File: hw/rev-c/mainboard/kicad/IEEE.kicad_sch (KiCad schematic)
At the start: 26 parts, among them J10 IEEE_HEADER, J11 IEEE, U14 SN74LS07, U15 SN74LS07, U16 SN74LS07, U17 74LS245, U18 74LS245

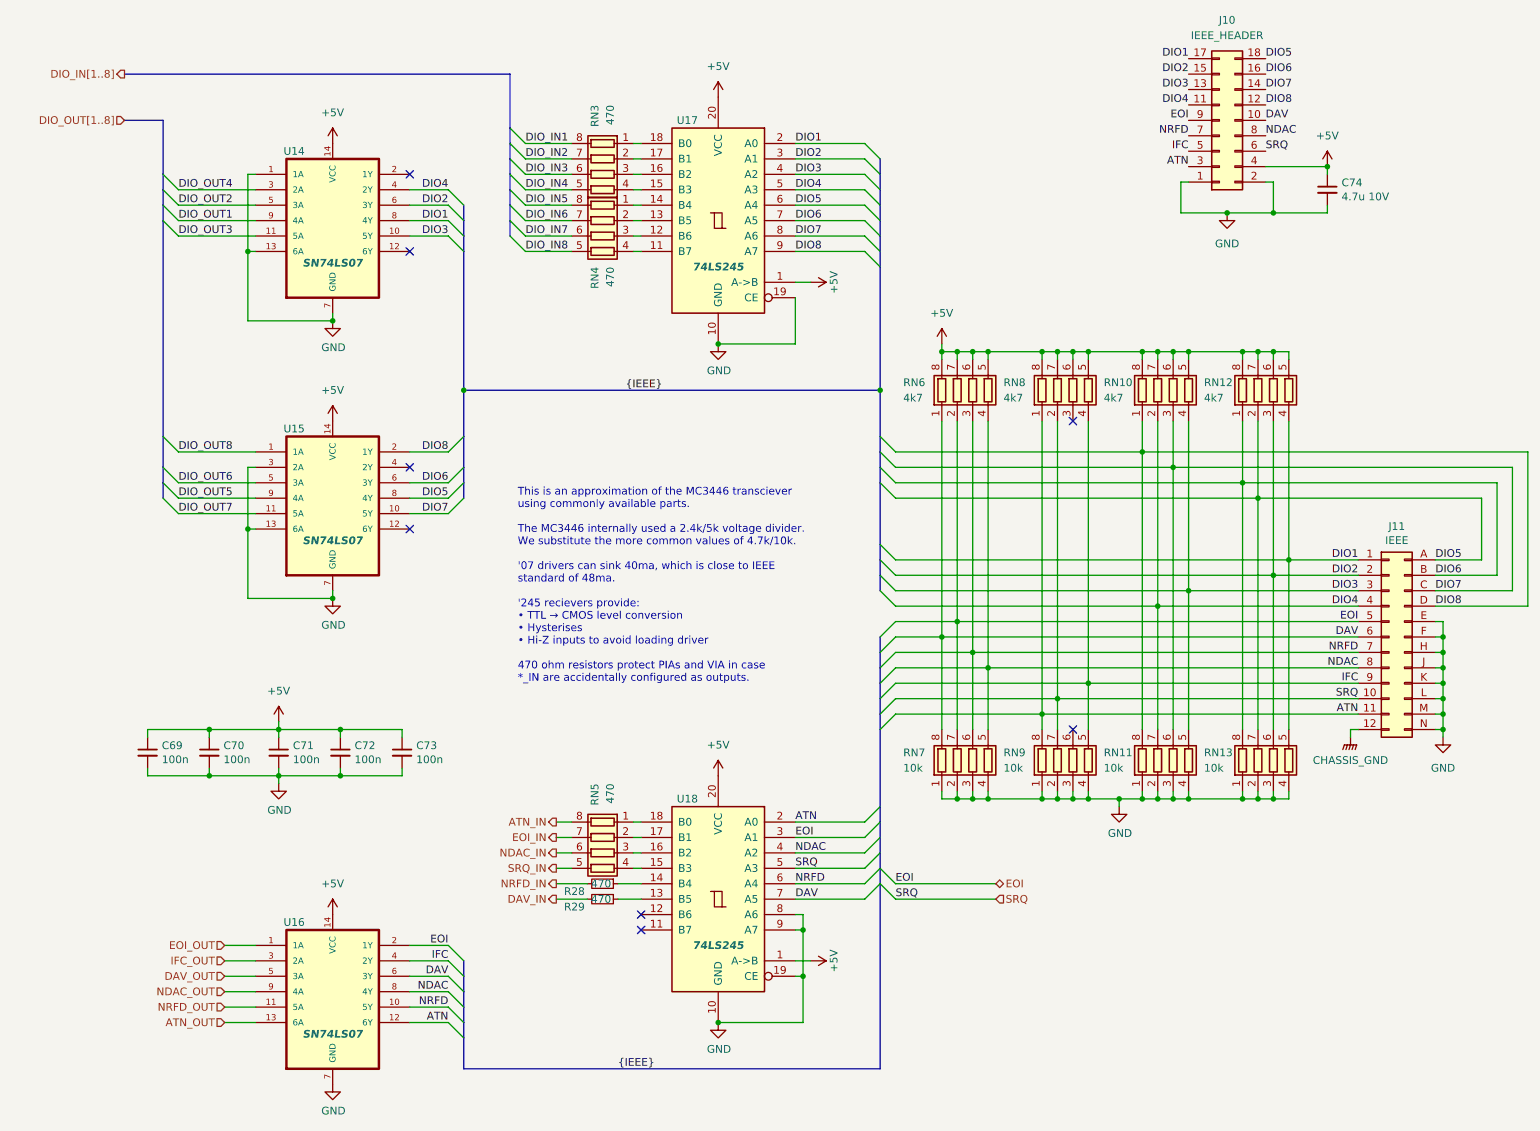
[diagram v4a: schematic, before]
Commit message: hw: match original PET designators for connectors
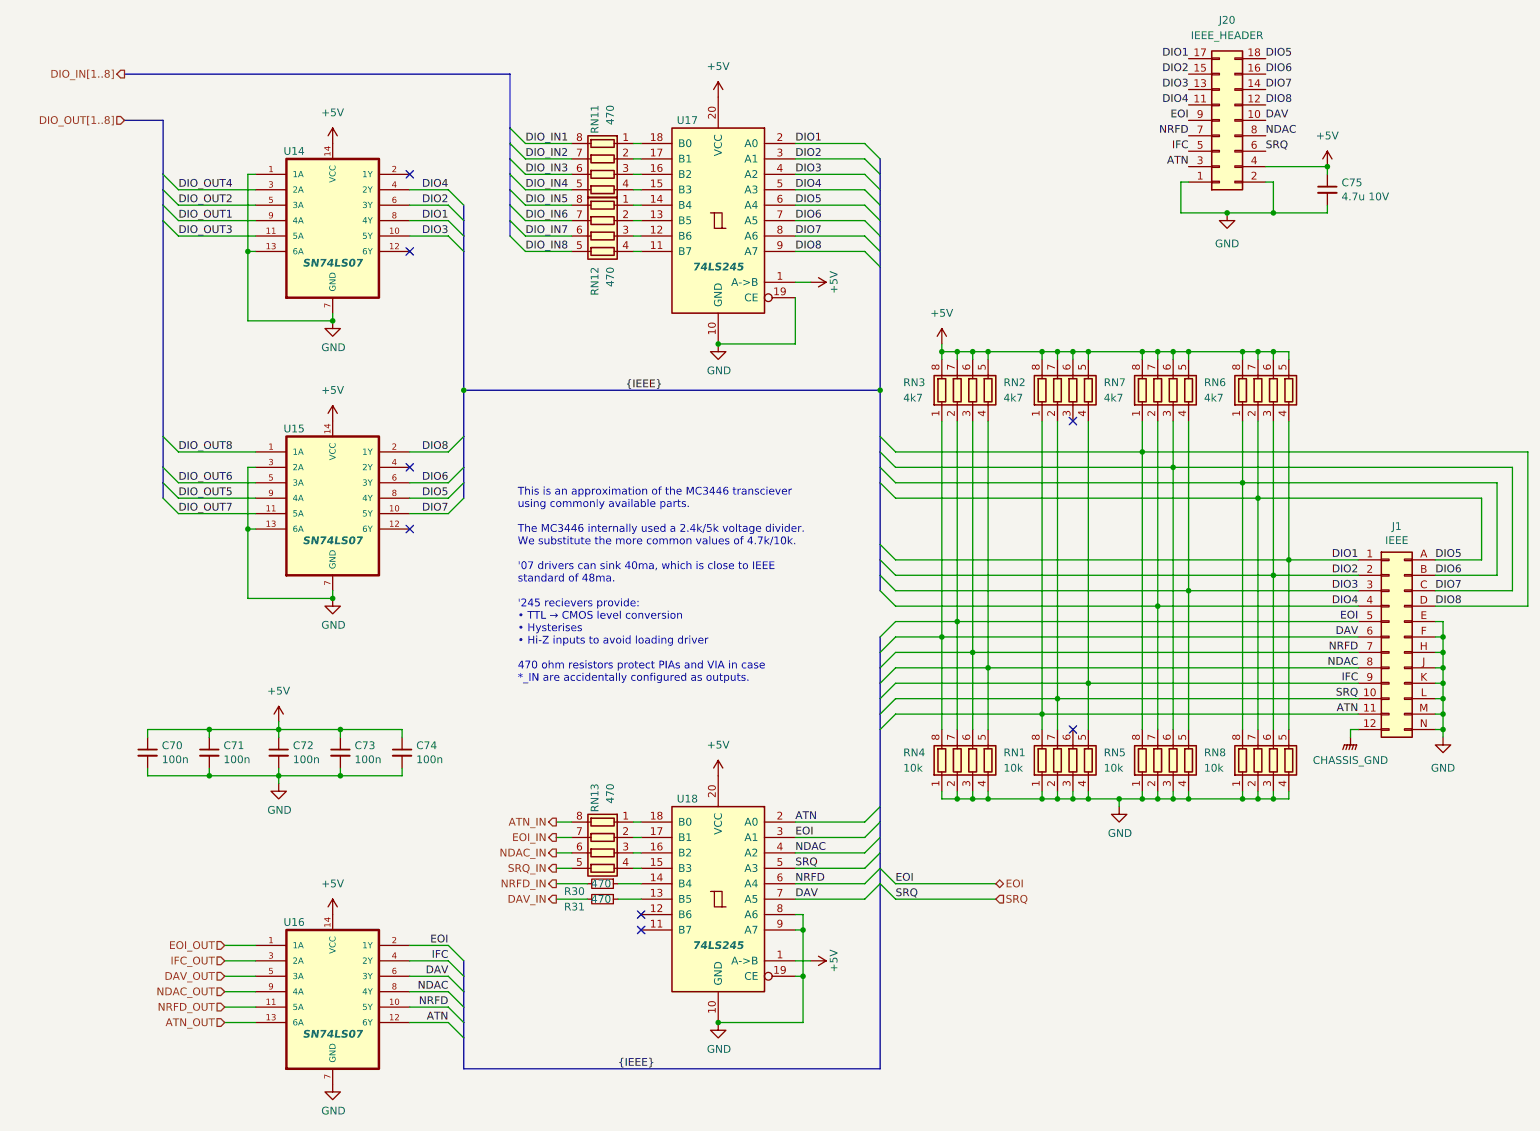
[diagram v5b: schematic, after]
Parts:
- renumbered C69 to C70, C70 to C71, C71 to C72, C72 to C73, C73 to C74, C74 to C75, J11 to J1, J10 to J20, R28 to R30, R29 to R31, RN9 to RN1, RN3 to RN11, RN4 to RN12, RN5 to RN13, RN8 to RN2, RN6 to RN3, RN7 to RN4, RN11 to RN5, RN12 to RN6, RN10 to RN7, RN13 to RN8
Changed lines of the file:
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@@
 		(on_board yes)
 		(dnp no)
-		(property "Reference" "C69"
+		(property "Reference" "C70"
 			(at 36.6268 137.2616 0)
 			(effects
@@
 			(project ""
 				(path "/2eea20e6-112c-411a-b615-885ae773135a/00000000-0000-0000-0000-00006151ec26"
-					(reference "C69")
+					(reference "C70")
 					(unit 1)
 				)
@@
 		(on_board yes)
 		(dnp no)
-		(property "Reference" "C70"
+		(property "Reference" "C71"
 			(at 46.7868 137.2616 0)
 			(effects
@@
 			(project ""
 				(path "/2eea20e6-112c-411a-b615-885ae773135a/00000000-0000-0000-0000-00006151ec26"
-					(reference "C70")
+					(reference "C71")
 					(unit 1)
 				)
@@
 		(on_board yes)
 		(dnp no)
-		(property "Reference" "C71"
+		(property "Reference" "C72"
 			(at 58.2168 137.2616 0)
 			(effects
@@
 			(project ""
 				(path "/2eea20e6-112c-411a-b615-885ae773135a/00000000-0000-0000-0000-00006151ec26"
-					(reference "C71")
+					(reference "C72")
 					(unit 1)
 				)
@@
 		(on_board yes)
 		(dnp no)
-		(property "Reference" "C72"
+		(property "Reference" "C73"
 			(at 68.3768 137.2616 0)
 			(effects
@@
 			(project ""
 				(path "/2eea20e6-112c-411a-b615-885ae773135a/00000000-0000-0000-0000-00006151ec26"
-					(reference "C72")
+					(reference "C73")
 					(unit 1)
 				)
@@
 		(on_board yes)
 		(dnp no)
-		(property "Reference" "C73"
+		(property "Reference" "C74"
 			(at 78.5368 137.2616 0)
 			(effects
@@
 			(project ""
 				(path "/2eea20e6-112c-411a-b615-885ae773135a/00000000-0000-0000-0000-00006151ec26"
-					(reference "C73")
+					(reference "C74")
 					(unit 1)
 				)
@@
 		(on_board yes)
 		(dnp no)
-		(property "Reference" "J11"
+		(property "Reference" "J1"
 			(at 240.03 101.1682 0)
 			(effects
@@
 			(project ""
 				(path "/2eea20e6-112c-411a-b615-885ae773135a/00000000-0000-0000-0000-00006151ec26"
-					(reference "J11")
+					(reference "J1")
 					(unit 1)
 				)
@@
 		(on_board yes)
 		(dnp no)
-		(property "Reference" "R28"
+		(property "Reference" "R30"
 			(at 102.87 161.29 90)
 			(effects
@@
 			(project ""
 				(path "/2eea20e6-112c-411a-b615-885ae773135a/00000000-0000-0000-0000-00006151ec26"
-					(reference "R28")
+					(reference "R30")
 					(unit 1)
 				)
@@
 		(on_board yes)
 		(dnp no)
-		(property "Reference" "RN4"
+		(property "Reference" "RN12"
 			(at 107.95 58.42 0)
 			(effects
@@
 			(project ""
 				(path "/2eea20e6-112c-411a-b615-885ae773135a/00000000-0000-0000-0000-00006151ec26"
-					(reference "RN4")
+					(reference "RN12")
 					(unit 1)
 				)
@@
 		(on_board yes)
 		(dnp no)
-		(property "Reference" "RN7"
+		(property "Reference" "RN4"
 			(at 158.75 138.43 0)
 			(effects
@@
 			(project ""
 				(path "/2eea20e6-112c-411a-b615-885ae773135a/00000000-0000-0000-0000-00006151ec26"
-					(reference "RN7")
+					(reference "RN4")
 					(unit 1)
 				)
@@
 		(on_board yes)
 		(dnp no)
-		(property "Reference" "RN13"
+		(property "Reference" "RN8"
 			(at 208.28 138.43 0)
 			(effects
@@
 			(project ""
 				(path "/2eea20e6-112c-411a-b615-885ae773135a/00000000-0000-0000-0000-00006151ec26"
-					(reference "RN13")
+					(reference "RN8")
 					(unit 1)
 				)
@@
 		(dnp no)
 		(fields_autoplaced yes)
-		(property "Reference" "J10"
+		(property "Reference" "J20"
 			(at 212.09 17.78 0)
 			(effects
@@
 			(project ""
 				(path "/2eea20e6-112c-411a-b615-885ae773135a/00000000-0000-0000-0000-00006151ec26"
-					(reference "J10")
+					(reference "J20")
 					(unit 1)
 				)
@@
 		(on_board yes)
 		(dnp no)
-		(property "Reference" "RN12"
+		(property "Reference" "RN6"
 			(at 208.28 77.47 0)
 			(effects
@@
 			(project ""
 				(path "/2eea20e6-112c-411a-b615-885ae773135a/00000000-0000-0000-0000-00006151ec26"
-					(reference "RN12")
+					(reference "RN6")
 					(unit 1)
 				)
@@
 		(on_board yes)
 		(dnp no)
-		(property "Reference" "RN3"
+		(property "Reference" "RN11"
 			(at 107.95 31.75 0)
 			(effects
@@
 			(project ""
 				(path "/2eea20e6-112c-411a-b615-885ae773135a/00000000-0000-0000-0000-00006151ec26"
-					(reference "RN3")
+					(reference "RN11")
 					(unit 1)
 				)
@@
 		(on_board yes)
 		(dnp no)
-		(property "Reference" "RN9"
+		(property "Reference" "RN1"
 			(at 175.26 138.43 0)
 			(effects
@@
 			(project ""
 				(path "/2eea20e6-112c-411a-b615-885ae773135a/00000000-0000-0000-0000-00006151ec26"
-					(reference "RN9")
+					(reference "RN1")
 					(unit 1)
 				)
@@
 		(on_board yes)
 		(dnp no)
-		(property "Reference" "RN5"
+		(property "Reference" "RN13"
 			(at 107.95 143.51 0)
 			(effects
@@
 			(project ""
 				(path "/2eea20e6-112c-411a-b615-885ae773135a/00000000-0000-0000-0000-00006151ec26"
-					(reference "RN5")
+					(reference "RN13")
 					(unit 1)
 				)
@@
 		(on_board yes)
 		(dnp no)
-		(property "Reference" "C74"
+		(property "Reference" "C75"
 			(at 230.9368 44.5516 0)
 			(effects
@@
 			(project ""
 				(path "/2eea20e6-112c-411a-b615-885ae773135a/00000000-0000-0000-0000-00006151ec26"
-					(reference "C74")
+					(reference "C75")
 					(unit 1)
 				)
@@
 		(on_board yes)
 		(dnp no)
-		(property "Reference" "RN8"
+		(property "Reference" "RN2"
 			(at 175.26 77.47 0)
 			(effects
@@
 			(project ""
 				(path "/2eea20e6-112c-411a-b615-885ae773135a/00000000-0000-0000-0000-00006151ec26"
-					(reference "RN8")
+					(reference "RN2")
 					(unit 1)
 				)
@@
 		(on_board yes)
 		(dnp no)
-		(property "Reference" "RN6"
+		(property "Reference" "RN3"
 			(at 158.75 77.47 0)
 			(effects
@@
 			(project ""
 				(path "/2eea20e6-112c-411a-b615-885ae773135a/00000000-0000-0000-0000-00006151ec26"
-					(reference "RN6")
+					(reference "RN3")
 					(unit 1)
 				)
@@
 		(on_board yes)
 		(dnp no)
-		(property "Reference" "R29"
+		(property "Reference" "R31"
 			(at 102.87 163.83 90)
 			(effects
@@
 			(project ""
 				(path "/2eea20e6-112c-411a-b615-885ae773135a/00000000-0000-0000-0000-00006151ec26"
-					(reference "R29")
+					(reference "R31")
 					(unit 1)
 				)
@@
 		(on_board yes)
 		(dnp no)
-		(property "Reference" "RN11"
+		(property "Reference" "RN5"
 			(at 191.77 138.43 0)
 			(effects
@@
 			(project ""
 				(path "/2eea20e6-112c-411a-b615-885ae773135a/00000000-0000-0000-0000-00006151ec26"
-					(reference "RN11")
+					(reference "RN5")
 					(unit 1)
 				)
@@
 		(on_board yes)
 		(dnp no)
-		(property "Reference" "RN10"
+		(property "Reference" "RN7"
 			(at 191.77 77.47 0)
 			(effects
@@
 			(project ""
 				(path "/2eea20e6-112c-411a-b615-885ae773135a/00000000-0000-0000-0000-00006151ec26"
-					(reference "RN10")
+					(reference "RN7")
 					(unit 1)
 				)

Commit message: hw: tidy warnings
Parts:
- J1: footprint Retrocomputing:CBM_PET_IEEE_EDGE_CON_24P -> EconoPET:CBM_PET_IEEE_EDGE_CON_24P
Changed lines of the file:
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@@
 			)
 		)
-		(property "Footprint" "Retrocomputing:CBM_PET_IEEE_EDGE_CON_24P"
+		(property "Footprint" "EconoPET:CBM_PET_IEEE_EDGE_CON_24P"
 			(at 238.76 119.38 0)
 			(effects

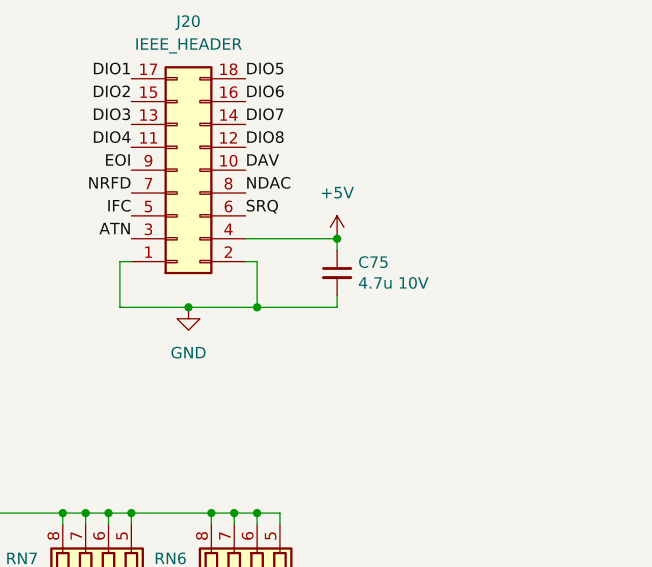
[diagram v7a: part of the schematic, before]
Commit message: hw: routing touchups, killer poke mitigation
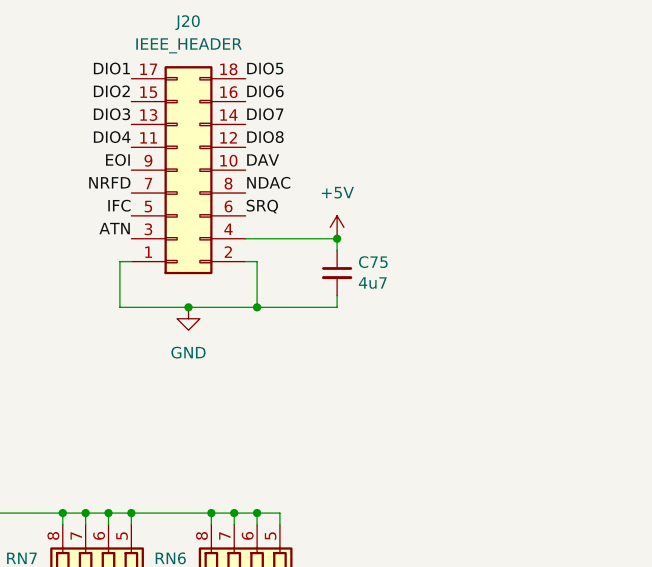
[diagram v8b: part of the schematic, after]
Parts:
- C75: value 4.7u 10V -> 4u7; LCSC C23733 -> C1538
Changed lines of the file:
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@@
 			)
 		)
-		(property "Value" "4.7u 10V"
+		(property "Value" "4u7"
 			(at 230.9368 46.863 0)
 			(effects
@@
 			)
 		)
-		(property "Datasheet" "https://product.samsungsem.com/mlcc/CL05A475MP5NRN.do"
+		(property "Datasheet" "https://www.lcsc.com/datasheet/lcsc_datasheet_2304140030_FH--Guangdong-Fenghua-Advanced-Tech-0402B472K500NT_C1538.pdf"
 			(at 228.6 45.72 0)
 			(effects
@@
 			)
 		)
-		(property "LCSC" "C23733"
+		(property "LCSC" "C1538"
 			(at 228.6 45.72 0)
 			(effects
